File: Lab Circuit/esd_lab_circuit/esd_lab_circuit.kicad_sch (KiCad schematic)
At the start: 7 parts, among them U3 74LS373, U4 RS232, U5 ATF16V8Bxx-xxPU, U6 M48Z35

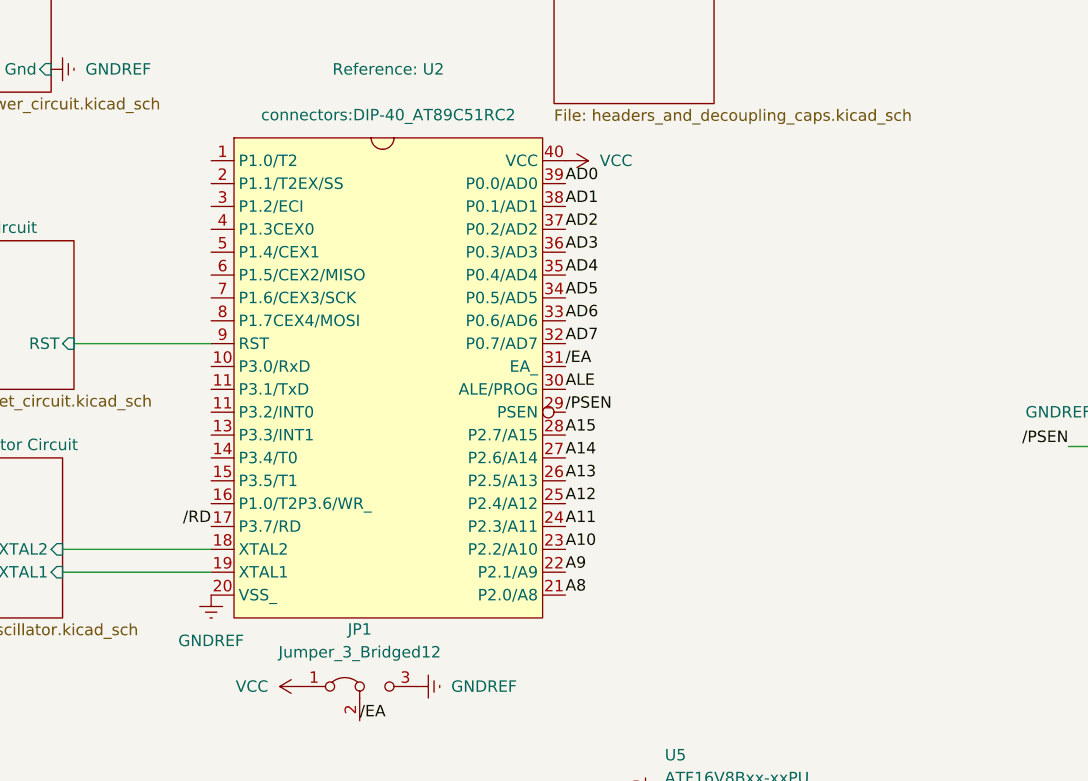
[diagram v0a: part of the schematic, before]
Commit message: Finished the timer with the recommended adjustment
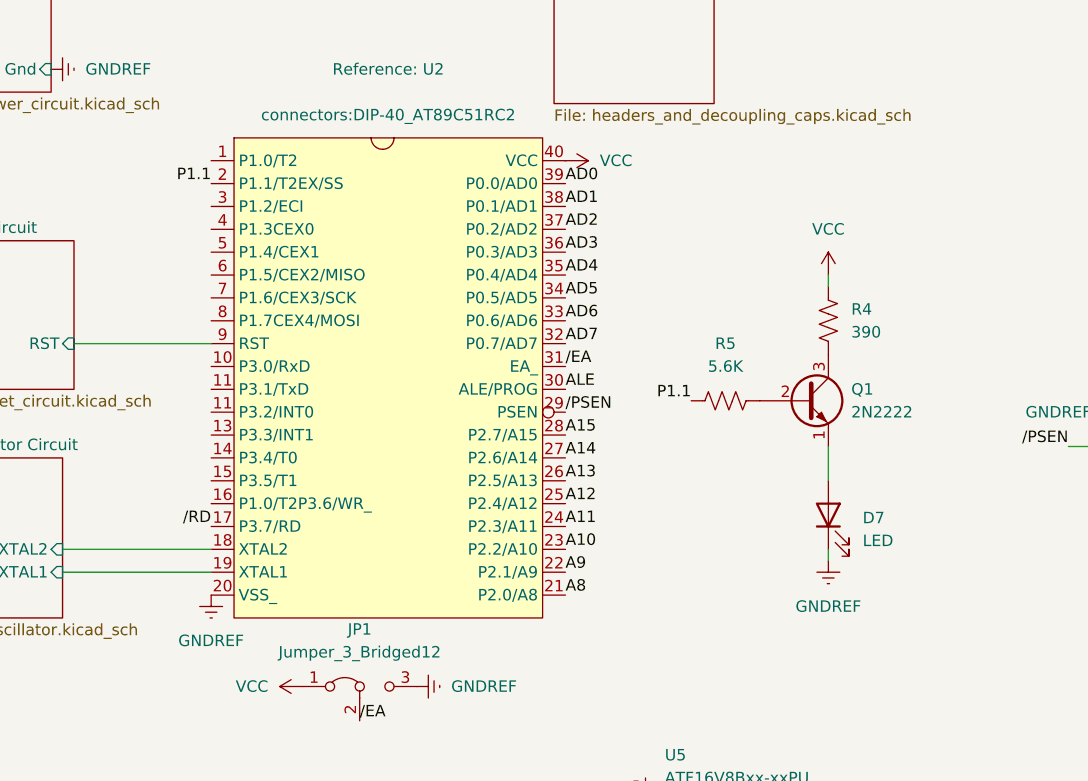
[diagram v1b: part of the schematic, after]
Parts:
- added D7: LED, symbol Device:LED
- added Q1: 2N2222, Package_TO_SOT_THT:TO-39-3, symbol ESD:2N2219
- added R4: 390, symbol Device:R_US
- added R5: 5.6K, symbol Device:R_US
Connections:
- net GNDREF: now also D7.1 (K)
- net VCC: now also R4.1
- net P1.1: now reaches U2.2 (P1.1/T2EX/SS)
- net P1.1: now also R5.2
- new net: Q1.3 (C), R4.2
- new net: Q1.2 (B), R5.1
- new net: D7.2 (A), Q1.1 (E)

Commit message: Got timing screenshots for part 1
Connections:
- net at U4.1 (DCD): now also U4.4 (DTR), U4.6 (DSR)
- net at U4.7 (RTS): now also U4.8 (CTS)
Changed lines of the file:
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@@
+		(color 0 0 0 0)
+	)
+	(junction
+		(at 259.08 34.29)
+		(diameter 0)
 		(color 0 0 0 0)
 	)
@@
 		(pts
 			(xy 139.7 71.12) (xy 144.78 71.12)
+		)
+		(stroke
+			(width 0)
+			(type default)
+		)
+	)
+	(wire
+		(pts
+			(xy 259.08 34.29) (xy 259.08 39.37)
+		)
+		(stroke
+			(width 0)
+			(type default)
+		)
+	)
+	(wire
+		(pts
+			(xy 260.35 44.45) (xy 261.62 44.45)
+		)
+		(stroke
+			(width 0)
+			(type default)
+		)
+	)
+	(wire
+		(pts
+			(xy 260.35 41.91) (xy 260.35 44.45)
+		)
+		(stroke
+			(width 0)
+			(type default)
+		)
+	)
+	(wire
+		(pts
+			(xy 261.62 26.67) (xy 259.08 26.67)
+		)
+		(stroke
+			(width 0)
+			(type default)
+		)
+	)
+	(wire
+		(pts
+			(xy 259.08 26.67) (xy 259.08 34.29)
+		)
+		(stroke
+			(width 0)
+			(type default)
+		)
+	)
+	(wire
+		(pts
+			(xy 261.62 34.29) (xy 259.08 34.29)
 		)
 		(stroke
@@
 		)
 		(stroke
+			(width 0)
+			(type default)
+		)
+	)
+	(wire
+		(pts
+			(xy 259.08 39.37) (xy 261.62 39.37)
+		)
+		(stroke
+			(width 0)
+			(type default)
+		)
+	)
+	(wire
+		(pts
+			(xy 261.62 41.91) (xy 260.35 41.91)
+		)
+		(stroke
